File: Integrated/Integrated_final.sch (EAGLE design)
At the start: 70 parts, among them IC1 74AHC1G32DBV, IC2 74AHC1G08DBV, IC3 74AHC1G08DBV, IC7 74AHC1G32DBV, Q1 PSMN013-30MLC, Q2 PSMN013-30MLC, Q3 PSMN013-30MLC, Q4 PSMN013-30MLC, Q5 PSMN013-30MLC, Q6 PSMN013-30MLC

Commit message: NO DRC ERROR!
YAY
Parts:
- removed R1: 10K, BeagleBone_Black_Wireless:R-US_M0805
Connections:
- net CSC renamed CSC_LOG
- removed net +3V3: JP1.15, JP5.15
- removed net D11(LOG): BRK_CONN.1, JP4.6, Q5.G, R9.2
- removed net N$26: Q3.G, R4.2
- new net !RESET_LOG: JP5.16
- new net AREF_LOG: JP5.14
- new net CAN_CS_LOG: JP4.9, LOGG_TRANS./CS
- new net CAN_INT_LOG: JP4.10, LOGG_TRANS./INT
- new net MISO_LOG: LOGG_TRANS.SO, SPI_LCD_CONN-6.1
- new net MOSI_LOG: LOGG_TRANS.SI, SPI_LCD_CONN-8.1
- new net SCK_LOG: LOGG_TRANS.SCK, SPI_LCD_CONN-7.1
- new net SCL_LOG: DASH_IN.4, IC7A.I0, JP4.11, R12.2
- new net SDA_LOG: DASH_IN.3, JP4.12, Q6.G, R6.2
- new net VBAT_LOG: JP4.1
- new net VBUS_LOG: JP4.3
- net !RESET: no longer JP5.16
- net 3.3V: now also IC1P.VCC, IC2P.VCC, IC3P.VCC, IC7P.VCC, JP5.15; no longer R1.1
- net AREF: no longer JP5.14
- net BRK: now also BRK_CONN.1, JP4.6, Q5.G, R9.2; no longer R1.2
- net CAN_CS: no longer JP4.9, LOGG_TRANS./CS
- net CAN_INT: no longer JP4.10, LOGG_TRANS./INT
- net D12(LOG): now also Q3.G, R4.2
- net GND: now also IC1P.GND, IC2P.GND, IC3P.GND, IC7P.GND
- net MISO: no longer LOGG_TRANS.SO, SPI_LCD_CONN-6.1
- net MOSI: no longer LOGG_TRANS.SI, SPI_LCD_CONN-8.1
- net SCK: no longer LOGG_TRANS.SCK, SPI_LCD_CONN-7.1
- net SCL: no longer DASH_IN.4, IC7A.I0, JP4.11, R12.2
- net SDA: no longer DASH_IN.3, JP4.12, Q6.G, R6.2
- net VBAT: no longer JP4.1
- net VBUS: no longer JP4.3

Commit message: Handing off for charlie's review
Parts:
- added X1, X2: 5566-4, con-molex:5566-4
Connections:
- net A0: now also X2-1.S
- net A3: now also X2-2.S
- net A4: now also X2-3.S
- net D0: now also X2-4.S
- net D10: now also X1-4.S
- net D11: now also X1-3.S
- net D12: now also X1-2.S
- net D13: now also X1-1.S
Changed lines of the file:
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@@
 <part name="SUPPLY35" library="SparkFun-Aesthetics" deviceset="12V" device=""/>
 <part name="+3V2" library="supply1" deviceset="+3V3" device=""/>
+<part name="X1" library="con-molex" library_urn="urn:adsk.eagle:library:165" deviceset="5566-4" device="" package3d_urn="urn:adsk.eagle:package:8078582/1"/>
+<part name="X2" library="con-molex" library_urn="urn:adsk.eagle:library:165" deviceset="5566-4" device="" package3d_urn="urn:adsk.eagle:package:8078582/1"/>
 </parts>
 <sheets>
@@
 <instance part="+3V2" gate="G$1" x="419.1" y="5.08" smashed="yes">
 <attribute name="VALUE" x="416.56" y="0" size="1.778" layer="96" rot="R90"/>
+</instance>
+<instance part="X1" gate="-1" x="647.7" y="22.86" smashed="yes">
+<attribute name="NAME" x="650.24" y="22.098" size="1.524" layer="95"/>
+<attribute name="VALUE" x="646.938" y="24.257" size="1.778" layer="96"/>
+</instance>
+<instance part="X1" gate="-2" x="647.7" y="20.32" smashed="yes">
+<attribute name="NAME" x="650.24" y="19.558" size="1.524" layer="95"/>
+</instance>
+<instance part="X1" gate="-3" x="647.7" y="17.78" smashed="yes">
+<attribute name="NAME" x="650.24" y="17.018" size="1.524" layer="95"/>
+</instance>
+<instance part="X1" gate="-4" x="647.7" y="15.24" smashed="yes">
+<attribute name="NAME" x="650.24" y="14.478" size="1.524" layer="95"/>
+</instance>
+<instance part="X2" gate="-1" x="647.7" y="7.62" smashed="yes">
+<attribute name="NAME" x="650.24" y="6.858" size="1.524" layer="95"/>
+<attribute name="VALUE" x="646.938" y="9.017" size="1.778" layer="96"/>
+</instance>
+<instance part="X2" gate="-2" x="647.7" y="5.08" smashed="yes">
+<attribute name="NAME" x="650.24" y="4.318" size="1.524" layer="95"/>
+</instance>
+<instance part="X2" gate="-3" x="647.7" y="2.54" smashed="yes">
+<attribute name="NAME" x="650.24" y="1.778" size="1.524" layer="95"/>
+</instance>
+<instance part="X2" gate="-4" x="647.7" y="0" smashed="yes">
+<attribute name="NAME" x="650.24" y="-0.762" size="1.524" layer="95"/>
 </instance>
 </instances>
@@
 <label x="599.44" y="-25.4" size="1.778" layer="95"/>
 </segment>
+<segment>
+<pinref part="X2" gate="-4" pin="S"/>
+<wire x1="645.16" y1="0" x2="640.08" y2="0" width="0.1524" layer="91"/>
+<label x="640.08" y="0" size="1.778" layer="95"/>
+</segment>
 </net>
 <net name="CAN_H" class="0">
@@
 <label x="599.44" y="-10.16" size="1.778" layer="95"/>
 </segment>
+<segment>
+<pinref part="X2" gate="-3" pin="S"/>
+<wire x1="645.16" y1="2.54" x2="640.08" y2="2.54" width="0.1524" layer="91"/>
+<label x="640.08" y="2.54" size="1.778" layer="95"/>
+</segment>
 </net>
 <net name="A3" class="0">
@@
 <label x="599.44" y="-7.62" size="1.778" layer="95"/>
 </segment>
+<segment>
+<pinref part="X2" gate="-2" pin="S"/>
+<wire x1="645.16" y1="5.08" x2="640.08" y2="5.08" width="0.1524" layer="91"/>
+<label x="640.08" y="5.08" size="1.778" layer="95"/>
+</segment>
 </net>
 <net name="RGN_BRK" class="0">
@@
 <label x="599.44" y="0" size="1.778" layer="95"/>
 </segment>
+<segment>
+<pinref part="X2" gate="-1" pin="S"/>
+<wire x1="645.16" y1="7.62" x2="640.08" y2="7.62" width="0.1524" layer="91"/>
+<label x="640.08" y="7.62" size="1.778" layer="95"/>
+</segment>
 </net>
 <net name="!RESET" class="0">
@@
 <pinref part="JP3" gate="G$1" pin="6"/>
 </segment>
+<segment>
+<pinref part="X1" gate="-3" pin="S"/>
+<wire x1="645.16" y1="17.78" x2="640.08" y2="17.78" width="0.1524" layer="91"/>
+<label x="640.08" y="17.78" size="1.778" layer="95"/>
+</segment>
 </net>
 <net name="D12" class="0">
@@
 <pinref part="JP3" gate="G$1" pin="5"/>
 </segment>
+<segment>
+<pinref part="X1" gate="-2" pin="S"/>
+<wire x1="645.16" y1="20.32" x2="640.08" y2="20.32" width="0.1524" layer="91"/>
+<label x="640.08" y="20.32" size="1.778" layer="95"/>
+</segment>
 </net>
 <net name="VBUS" class="0">
@@
 <pinref part="JP3" gate="G$1" pin="4"/>
 </segment>
+<segment>
+<pinref part="X1" gate="-1" pin="S"/>
+<wire x1="645.16" y1="22.86" x2="640.08" y2="22.86" width="0.1524" layer="91"/>
+<label x="640.08" y="22.86" size="1.778" layer="95"/>
+</segment>
 </net>
 <net name="SCL" class="0">
@@
 <pinref part="JP3" gate="G$1" pin="7"/>
 </segment>
-</net>
+<segment>
+<pinref part="X1" gate="-4" pin="S"/>
+<wire x1="645.16" y1="15.24" x2="640.08" y2="15.24" width="0.1524" layer="91"/>
+<label x="640.08" y="15.24" size="1.778" layer="95"/>
+</segment>
+</net>

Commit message: removed some dimensions that were on the copper layer, checked pinning. TODO: fix CAN pinout on the CAN interface connectors, follow linus' BMS issues
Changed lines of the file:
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@@
 <?xml version="1.0" encoding="utf-8"?>
 <!DOCTYPE eagle SYSTEM "eagle.dtd">
-<eagle version="9.5.2">
+<eagle version="9.1.3">
 <drawing>
 <settings>
@@
 <attribute name="VALUE" x="221.615" y="-51.435" size="1.778" layer="96"/>
 </instance>
-<instance part="SUPPLY29" gate="GND" x="220.98" y="12.7" smashed="yes">
-<attribute name="VALUE" x="219.075" y="9.525" size="1.778" layer="96"/>
+<instance part="SUPPLY29" gate="GND" x="213.36" y="10.16" smashed="yes">
+<attribute name="VALUE" x="211.455" y="6.985" size="1.778" layer="96"/>
 </instance>
 <instance part="R13" gate="G$1" x="195.58" y="22.86" smashed="yes" rot="R90">
@@
 <attribute name="VALUE" x="206.502" y="-46.99" size="1.778" layer="96" rot="R90"/>
 </instance>
-<instance part="SUPPLY32" gate="GND" x="203.2" y="-48.26" smashed="yes">
-<attribute name="VALUE" x="201.295" y="-51.435" size="1.778" layer="96"/>
+<instance part="SUPPLY32" gate="GND" x="198.12" y="-50.8" smashed="yes">
+<attribute name="VALUE" x="196.215" y="-53.975" size="1.778" layer="96"/>
 </instance>
 <instance part="IC1" gate="A" x="241.3" y="25.4" smashed="yes">
@@
 </segment>
 <segment>
+<pinref part="SUPPLY35" gate="G$1" pin="12V"/>
+<wire x1="198.12" y1="60.96" x2="198.12" y2="63.5" width="0.1524" layer="91"/>
 <pinref part="HD_LED" gate="G$1" pin="2"/>
 <pinref part="HD_LED1" gate="G$1" pin="2"/>
@@
 <wire x1="134.62" y1="50.8" x2="154.94" y2="50.8" width="0.1524" layer="91"/>
 <wire x1="154.94" y1="50.8" x2="154.94" y2="60.96" width="0.1524" layer="91"/>
-<wire x1="154.94" y1="60.96" x2="208.28" y2="60.96" width="0.1524" layer="91"/>
+<wire x1="154.94" y1="60.96" x2="198.12" y2="60.96" width="0.1524" layer="91"/>
+<wire x1="198.12" y1="60.96" x2="208.28" y2="60.96" width="0.1524" layer="91"/>
 <wire x1="208.28" y1="60.96" x2="208.28" y2="48.26" width="0.1524" layer="91"/>
 <pinref part="RT_LED1" gate="G$1" pin="2"/>
@@
 <junction x="327.66" y="-7.62"/>
 <junction x="317.5" y="-7.62"/>
-</segment>
-<segment>
-<pinref part="SUPPLY35" gate="G$1" pin="12V"/>
-<wire x1="198.12" y1="60.96" x2="198.12" y2="63.5" width="0.1524" layer="91"/>
+<junction x="198.12" y="60.96"/>
+<junction x="198.12" y="63.5"/>
 </segment>
 <segment>
@@
 <wire x1="541.02" y1="111.76" x2="541.02" y2="104.14" width="0.1524" layer="91"/>
 <label x="541.02" y="111.76" size="1.778" layer="95"/>
+<junction x="541.02" y="104.14"/>
 </segment>
 <segment>
@@
 <junction x="210.82" y="-15.24"/>
 <pinref part="C12" gate="G$1" pin="2"/>
+<junction x="213.36" y="-15.24"/>
 </segment>
 <segment>
@@
 <pinref part="R10" gate="G$1" pin="1"/>
 <pinref part="SUPPLY29" gate="GND" pin="GND"/>
-<wire x1="220.98" y1="15.24" x2="220.98" y2="12.7" width="0.1524" layer="91"/>
+<wire x1="213.36" y1="12.7" x2="220.98" y2="12.7" width="0.1524" layer="91"/>
 </segment>
 <segment>
@@
 <pinref part="R12" gate="G$1" pin="1"/>
 <pinref part="SUPPLY32" gate="GND" pin="GND"/>
-<wire x1="203.2" y1="-48.26" x2="203.2" y2="-45.72" width="0.1524" layer="91"/>
+<wire x1="203.2" y1="-48.26" x2="198.12" y2="-48.26" width="0.1524" layer="91"/>
 </segment>
 <segment>
@@
 <wire x1="307.34" y1="22.86" x2="312.42" y2="22.86" width="0.1524" layer="91"/>
 <pinref part="Q4" gate="G$1" pin="G"/>
+<junction x="307.34" y="22.86"/>
 </segment>
 </net>
@@
 <wire x1="307.34" y1="-30.48" x2="312.42" y2="-30.48" width="0.1524" layer="91"/>
 <pinref part="Q2" gate="G$1" pin="G"/>
+<junction x="307.34" y="-30.48"/>
 </segment>
 </net>
@@
 <wire x1="124.46" y1="-25.4" x2="134.62" y2="-25.4" width="0.1524" layer="91"/>
 <pinref part="Q6" gate="G$1" pin="D"/>
-</segment>
-</net>
+<junction x="134.62" y="-25.4"/>
+</segment>
+</net>

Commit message: ok i think its finally done
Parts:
- removed F2: SMD-MICRO-FUSE-BLOCK, f-lf-omniblok-s:SMD-MICRO-FUSE-BLOCK
- added F1: SMD-MICRO-FUSE-BLOCK, f-lf-omniblok-s:SMD-MICRO-FUSE-BLOCK
- added R1, R15: 0, rcl:R-US_R0805
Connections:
- removed net CAN+: CAN_CONN_IN.4, CAN_CONN_OUT.4, F2.1
- new net CAN_SHIELD: CAN_CONN_OUT.1, R15.2
- new net CAN_SHIELD_2: CAN_CONN_IN.1, R1.2
- net 12V: now also CAN_CONN_IN.2, CAN_CONN_OUT.2, F1.1, F1.2; no longer CAN_CONN_IN.1, CAN_CONN_OUT.1, F2.2
- net CAN_H: now also CAN_CONN_IN.4, CAN_CONN_OUT.4; no longer CAN_CONN_IN.5, CAN_CONN_OUT.5
- net CAN_L: now also CAN_CONN_IN.5, CAN_CONN_OUT.5; no longer CAN_CONN_IN.2, CAN_CONN_OUT.2
- net GND: now also R1.1, R15.1

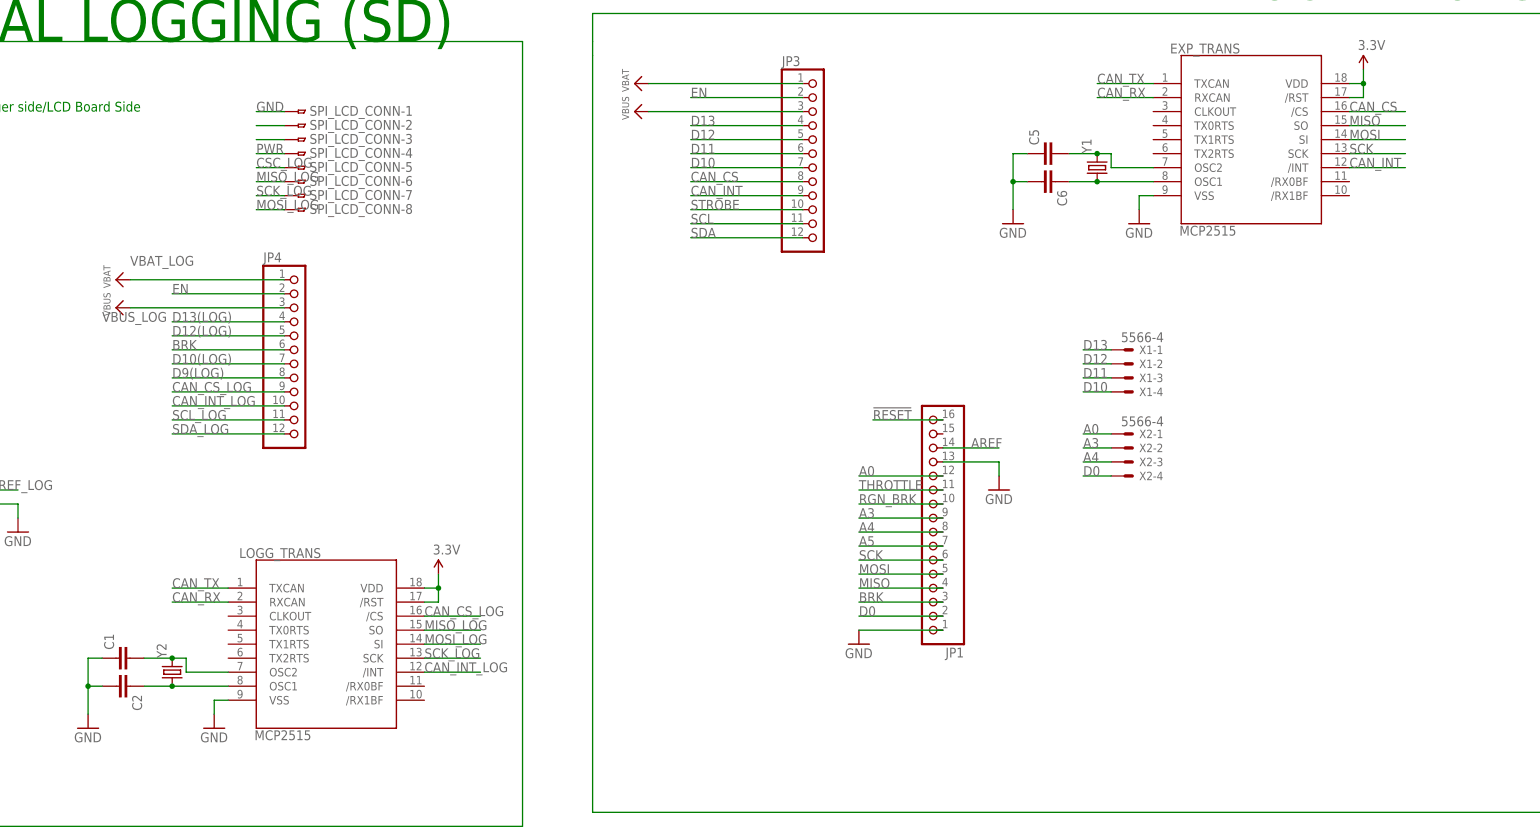
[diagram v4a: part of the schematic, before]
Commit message: changed connectors to spare digital and analog to 90 degree 4 pin molex minifit
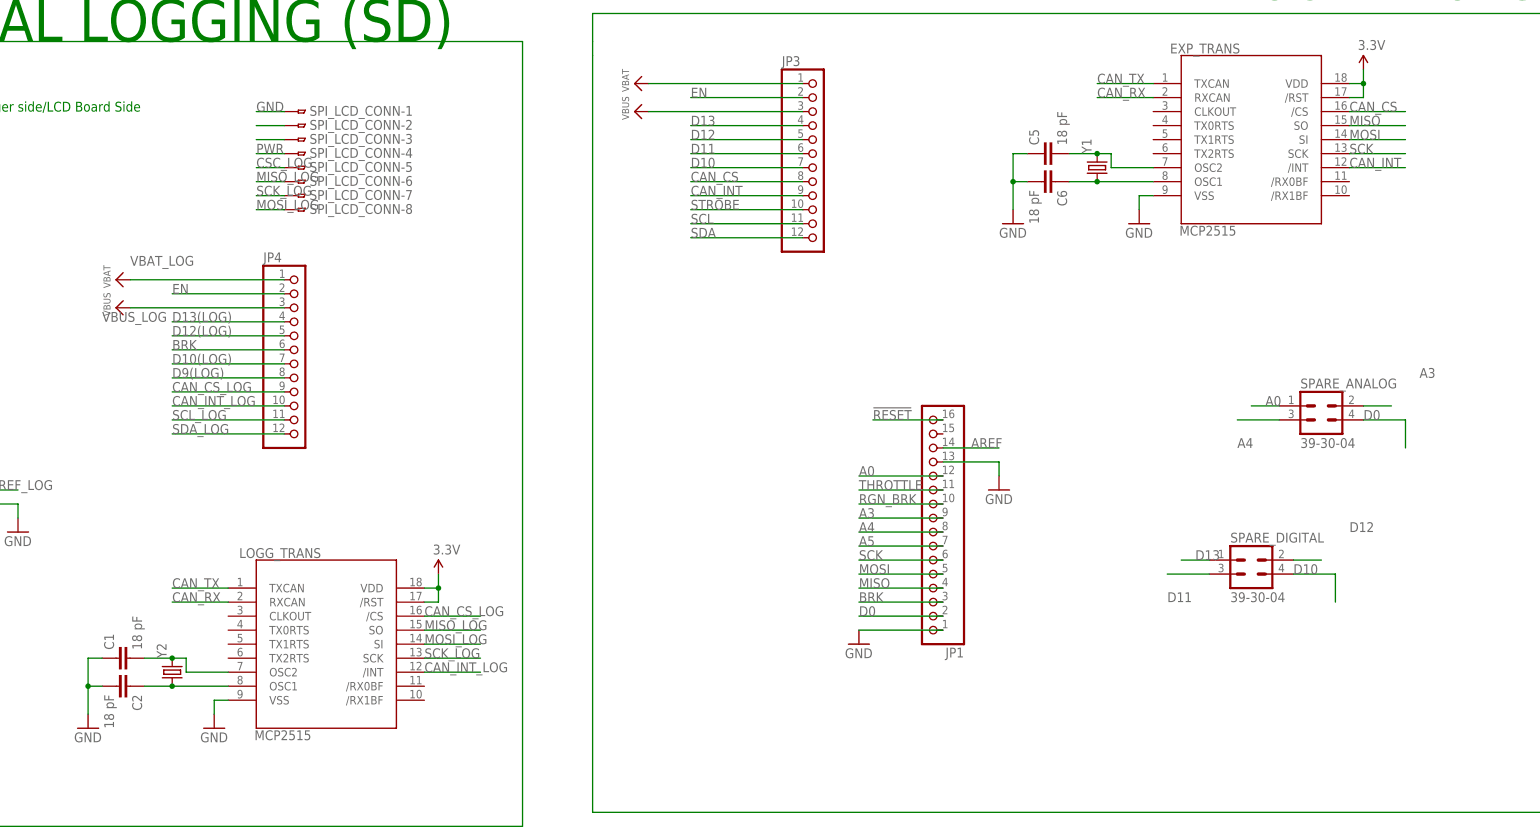
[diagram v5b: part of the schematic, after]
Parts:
- removed X1, X2: 5566-4, con-molex:5566-4
- added SPARE_ANALOG, SPARE_DIGITAL: 39-30-04, con-molex-mini-fit:39-30-04
- C1, C2, C5, C6: value (none) -> 18 pF
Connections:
- net A0: now also SPARE_ANALOG.1; no longer X2-1.S
- net A3: now also SPARE_ANALOG.2; no longer X2-2.S
- net A4: now also SPARE_ANALOG.3; no longer X2-3.S
- net D0: now also SPARE_ANALOG.4; no longer X2-4.S
- net D10: now also SPARE_DIGITAL.4; no longer X1-4.S
- net D11: now also SPARE_DIGITAL.3; no longer X1-3.S
- net D12: now also SPARE_DIGITAL.2; no longer X1-2.S
- net D13: now also SPARE_DIGITAL.1; no longer X1-1.S
